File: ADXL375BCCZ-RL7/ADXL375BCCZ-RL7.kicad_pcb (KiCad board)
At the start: 2 copper layers, 17.4 x 11.6 mm, 6 parts, among them J1 Conn_01x04_Pin, J2 Conn_01x04_Pin, U7 ADXL375BCCZ-RL7

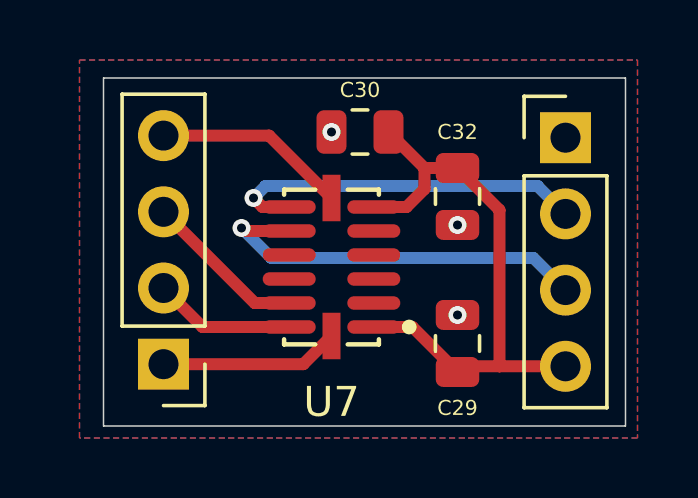
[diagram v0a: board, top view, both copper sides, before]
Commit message: add silkscreen
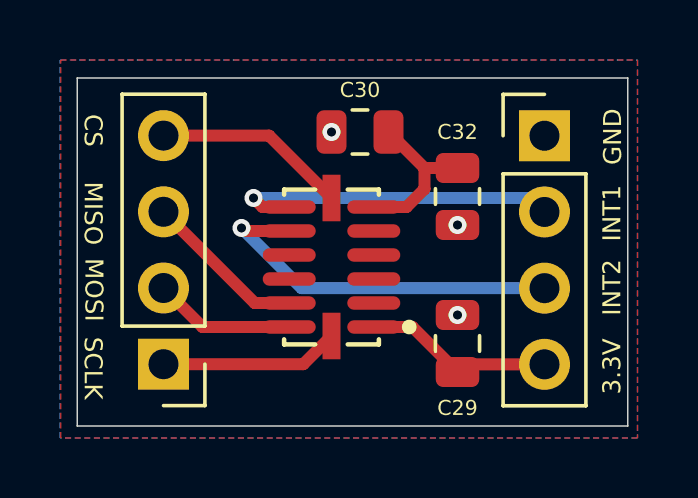
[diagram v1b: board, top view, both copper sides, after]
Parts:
- moved J2 0.70 mm to (145.1, 74.3)
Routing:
- net +3.3V: track 19.7 -> 11.9 mm
- net ADXL375_INT1: track 12.3 -> 11.2 mm
- net ADXL375_INT2: track 13.3 -> 12.6 mm
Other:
- board size 17.4 x 11.6 mm -> 18.3 x 11.6 mm
- board text added: "3.3V"
- board text added: "CS"
- board text added: "GND"
- board text added: "INT1"
- board text added: "INT2"
- board text added: "MISO"
- board text added: "MOSI"
- board text added: "SCLK"
